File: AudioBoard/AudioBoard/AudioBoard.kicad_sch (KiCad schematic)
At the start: 0 parts

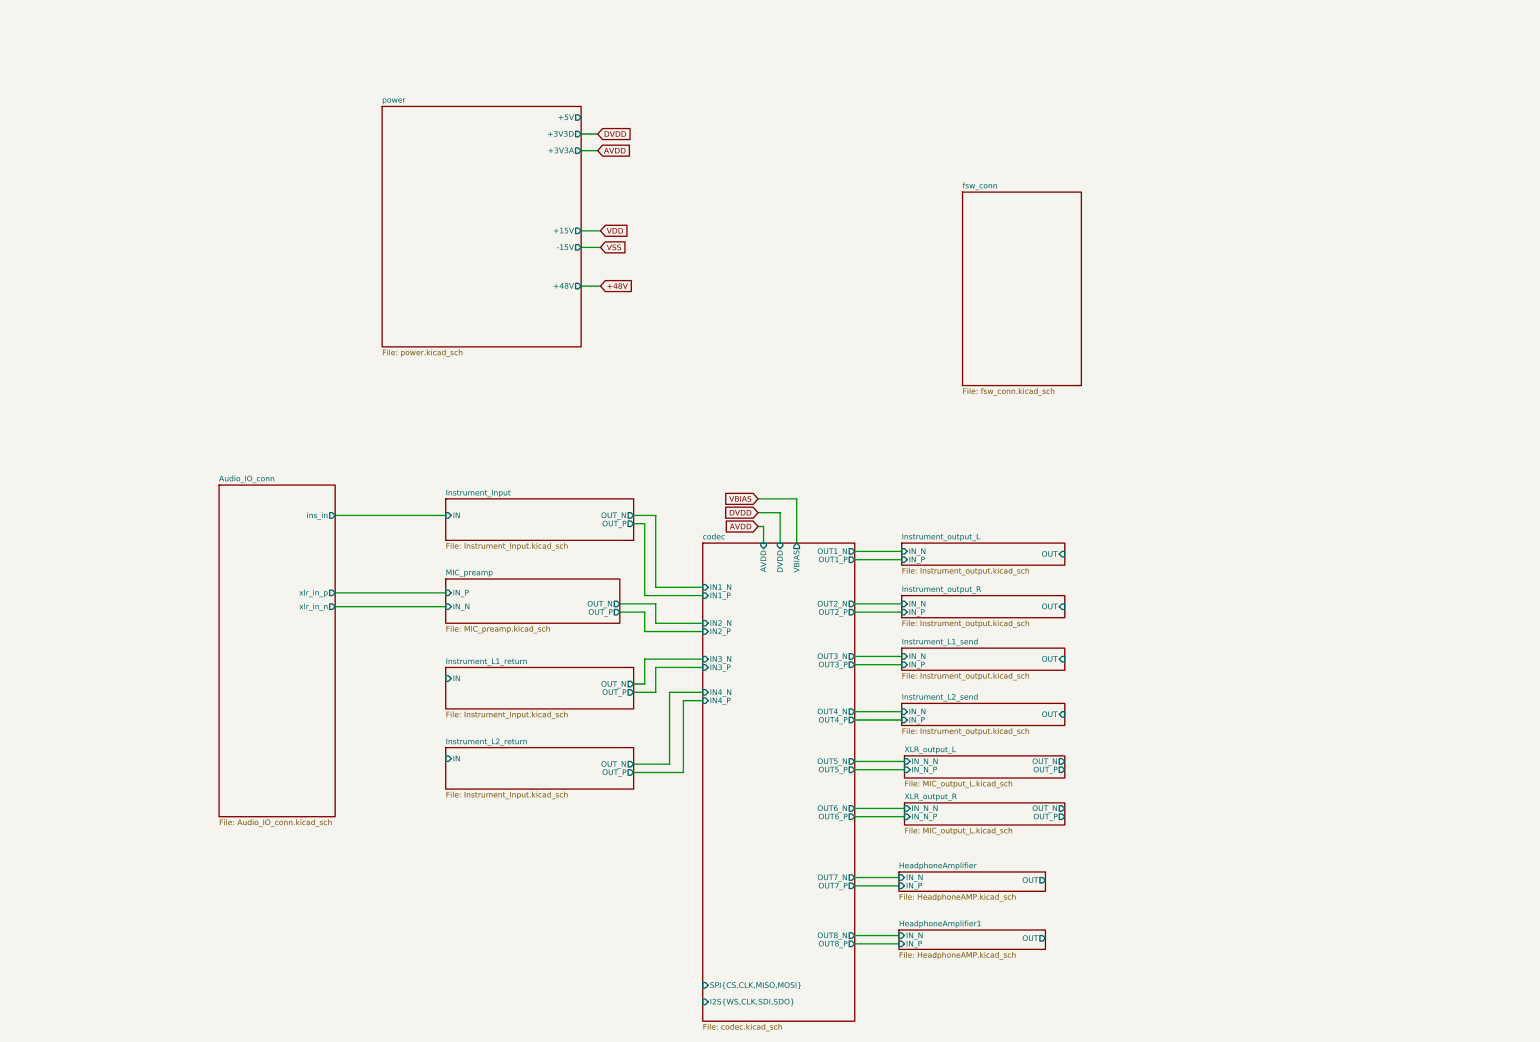
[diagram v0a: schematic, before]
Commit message: added first time routing to see crosssections
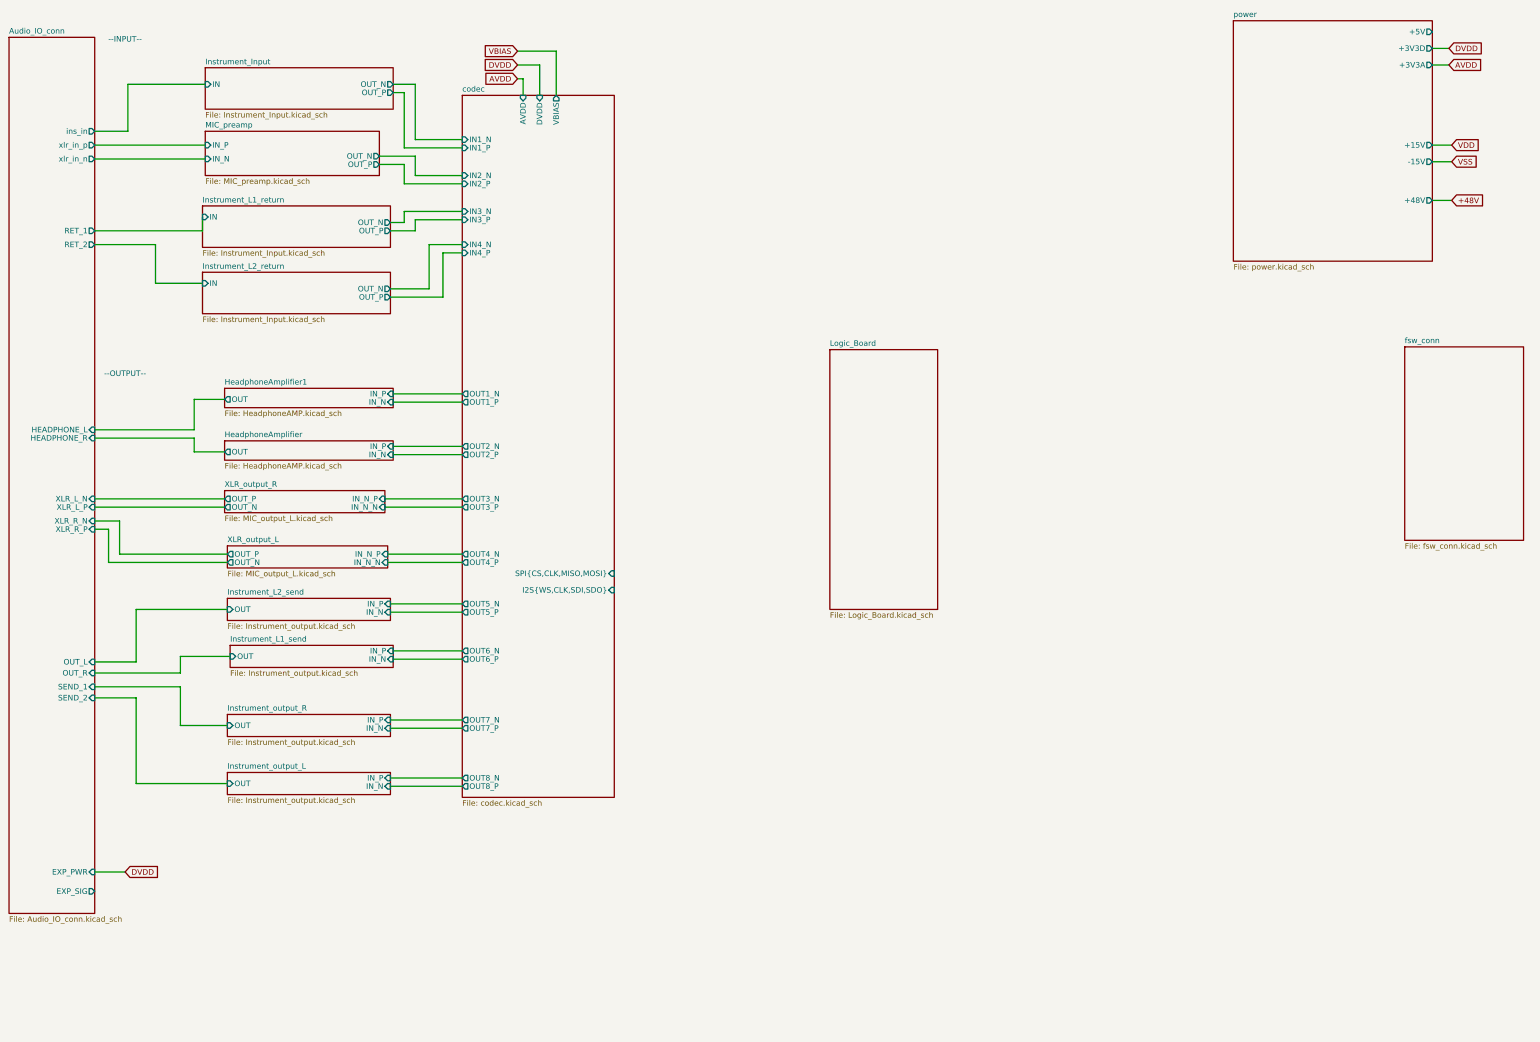
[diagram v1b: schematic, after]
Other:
- added sheet Logic_Board (Logic_Board.kicad_sch)
- sheet Audio_IO_conn ports: added EXP_PWR, EXP_SIG, HEADPHONE_L, HEADPHONE_R, OUT_L, OUT_R, RET_1, RET_2, SEND_1, SEND_2, XLR_L_N, XLR_L_P, XLR_R_N, XLR_R_P; removed none
- note added: "--INPUT--"
- note added: "--OUTPUT--"

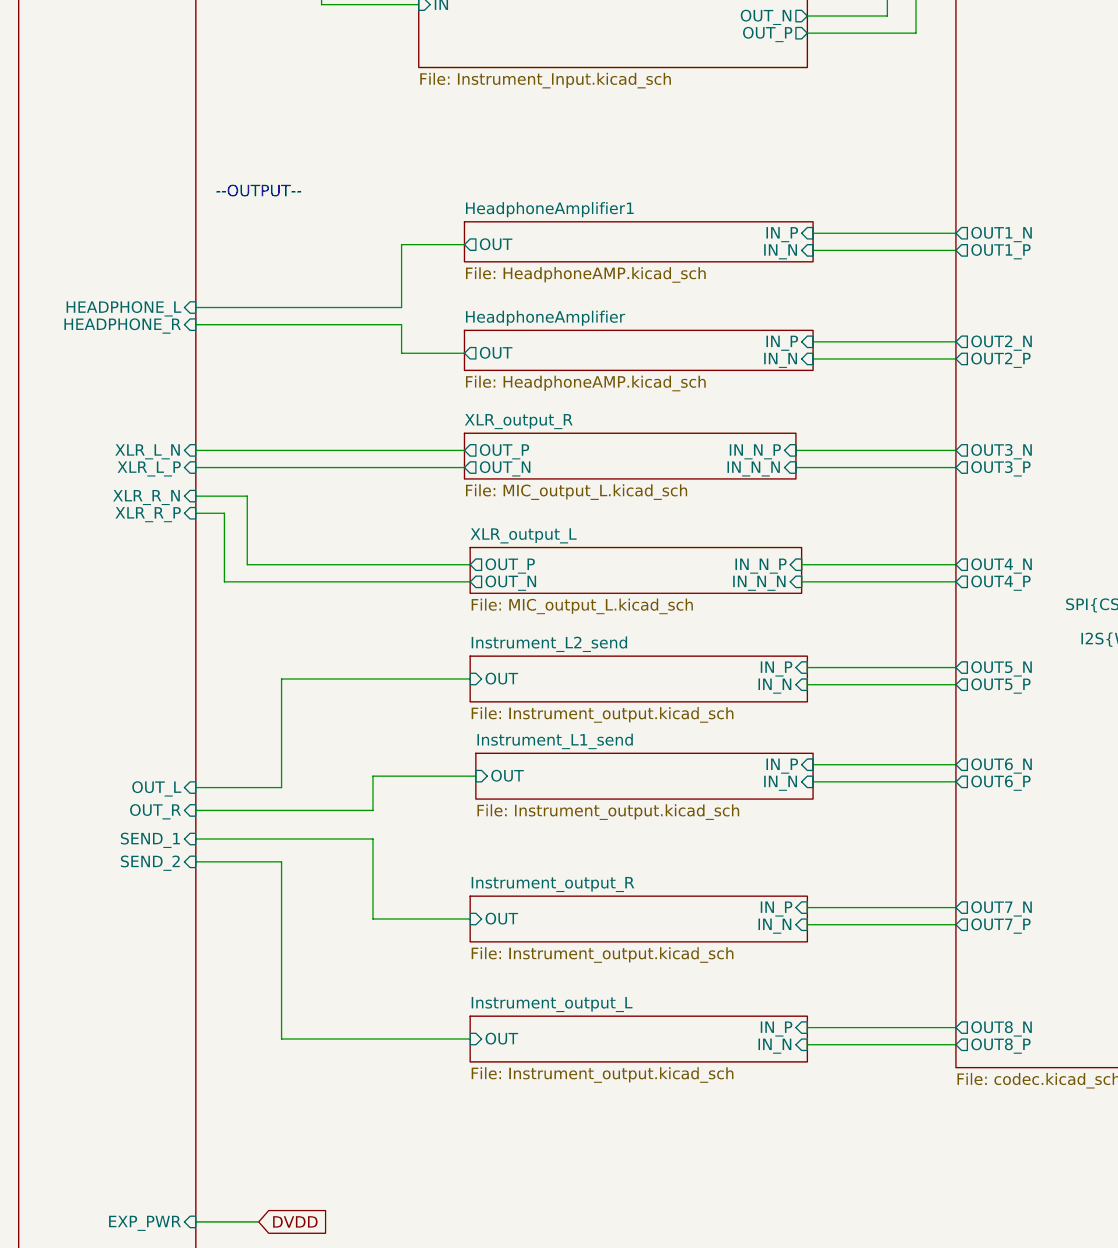
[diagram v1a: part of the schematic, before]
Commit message: optimized codec layout
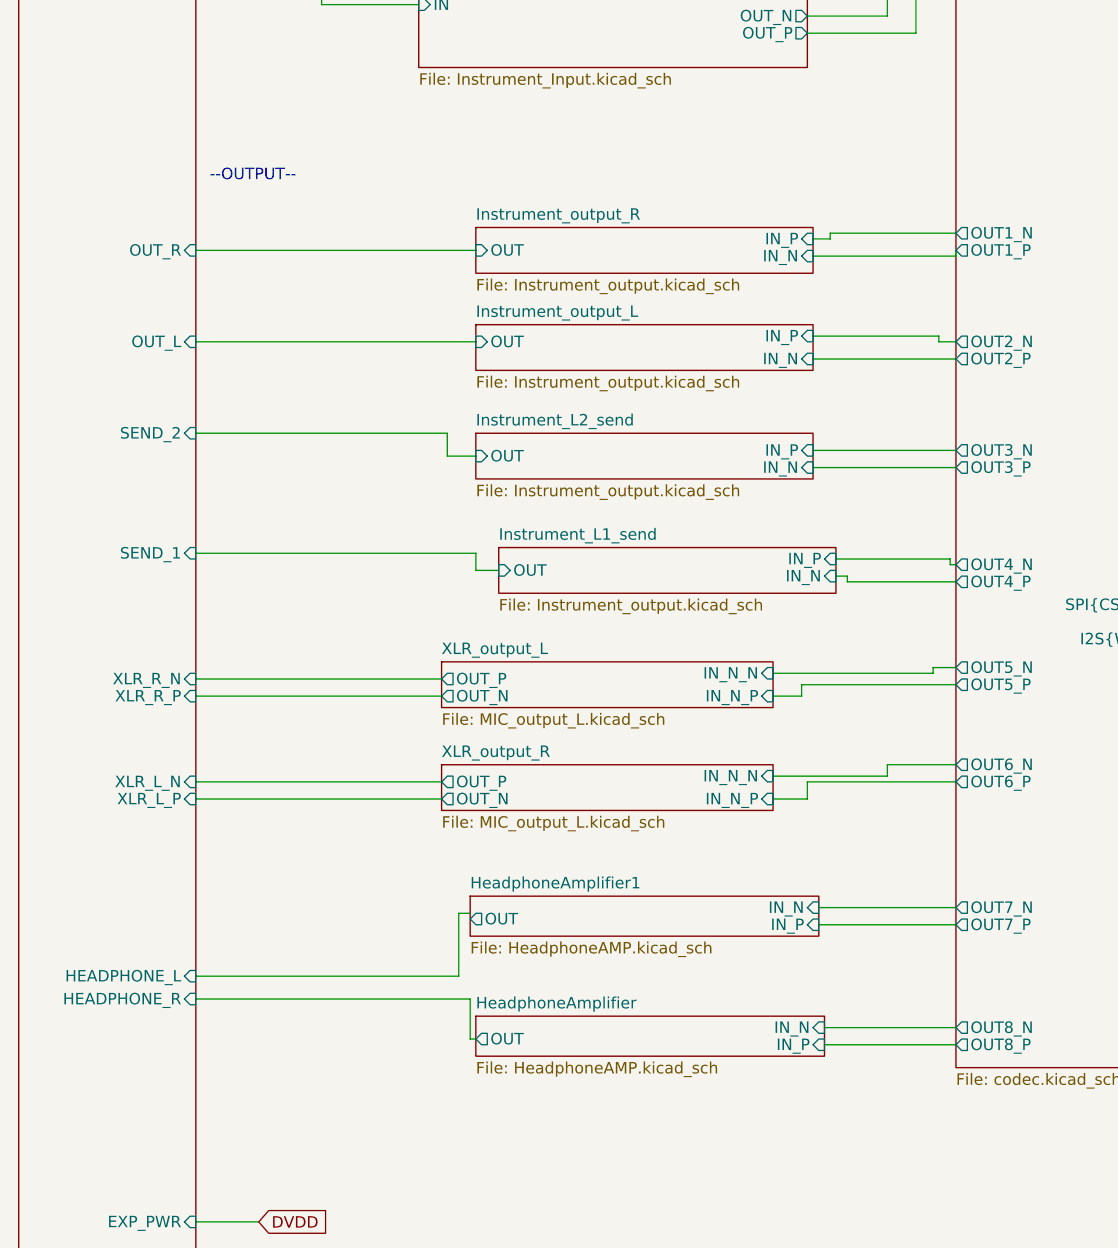
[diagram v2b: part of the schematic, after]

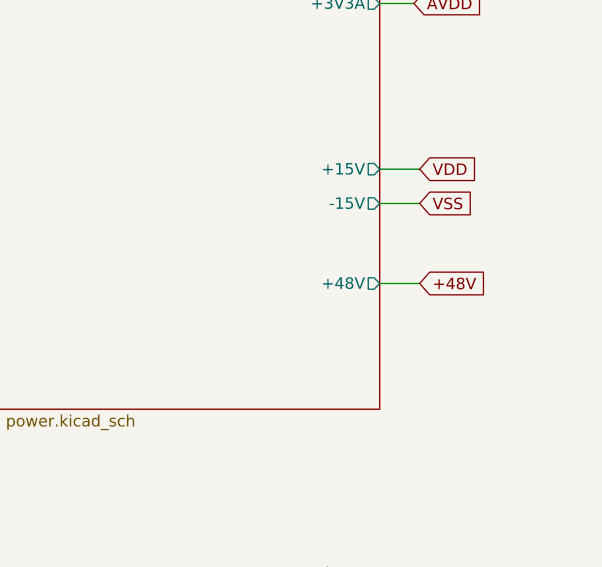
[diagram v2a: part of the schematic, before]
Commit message: added power electronics
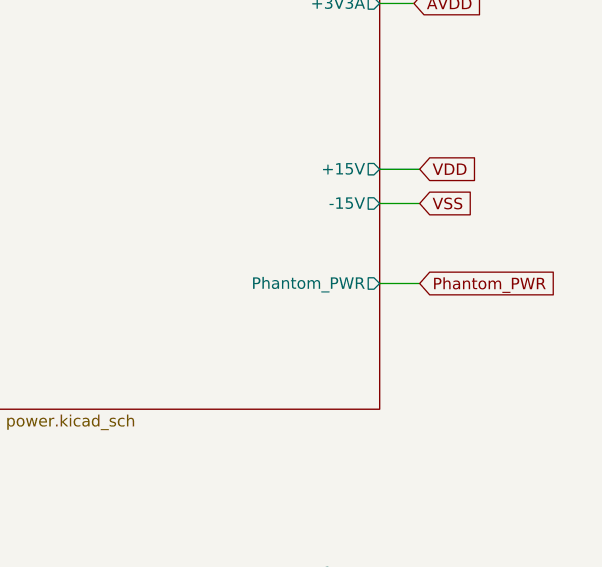
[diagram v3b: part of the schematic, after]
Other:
- sheet power ports: added Phantom_PWR; removed +48V
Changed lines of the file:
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@@
 		)
 	)
-	(global_label "+48V"
+	(global_label "Phantom_PWR"
 		(shape input)
 		(at 365.125 61.595 0)
@@
 		)
 		(property "Intersheetrefs" "${INTERSHEET_REFS}"
-			(at 373.1902 61.595 0)
+			(at 381.3542 61.595 0)
 			(hide yes)
 			(show_name no)
@@
 			)
 		)
-		(pin "+48V" output
-			(at 360.68 61.595 0)
-			(effects
-				(font
-					(size 1.27 1.27)
-				)
-				(justify right)
-			)
-		)
 		(pin "+3V3A" output
 			(at 360.68 30.48 0)
@@
 			(effects
 				(font
+					(size 1.27 1.27)
+				)
+				(justify right)
+			)
+		)
+		(pin "Phantom_PWR" output
+			(at 360.68 61.595 0)
+			(effects
+				(font

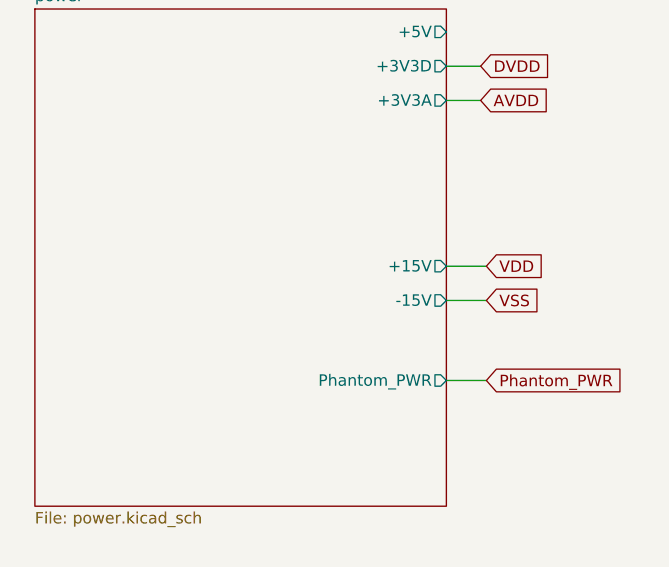
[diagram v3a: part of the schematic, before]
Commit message: added power protection, dcdc modules
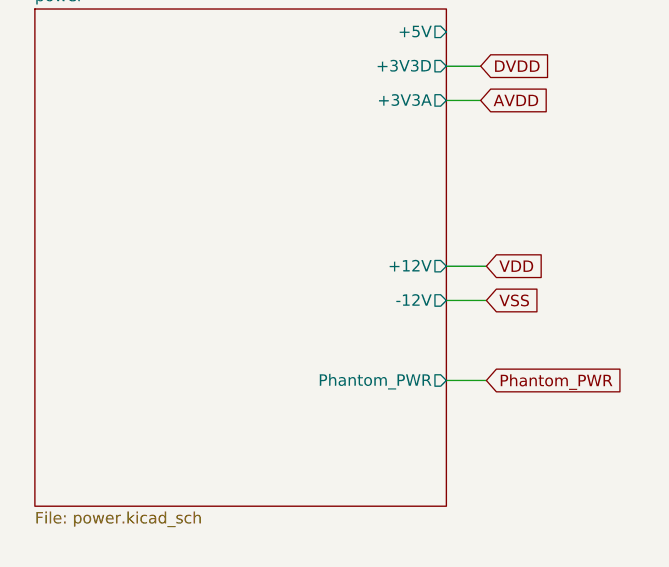
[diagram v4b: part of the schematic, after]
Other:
- sheet power ports: added +12V, -12V; removed +15V, -15V
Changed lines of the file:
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@@
 			)
 		)
-		(pin "+15V" output
+		(pin "+12V" output
 			(at 360.68 48.895 0)
 			(effects
@@
 			)
 		)
-		(pin "-15V" output
+		(pin "-12V" output
 			(at 360.68 52.705 0)
 			(effects
